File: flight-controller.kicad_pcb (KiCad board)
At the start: 4 copper layers, 36 x 36 mm, 61 parts, among them J1 USB_C_Receptacle_USB2.0, Q1 AO3400A, SW1 SW_Push, U1 AT32F435RGT7, U2 BMI270, U3 BMP280, U4 W25N01GVZEIG, U5 AT7456E, U6 TPS54302, U7 TPS54302, U8 TLV75733PDBV, U9 USBLC6-2P6

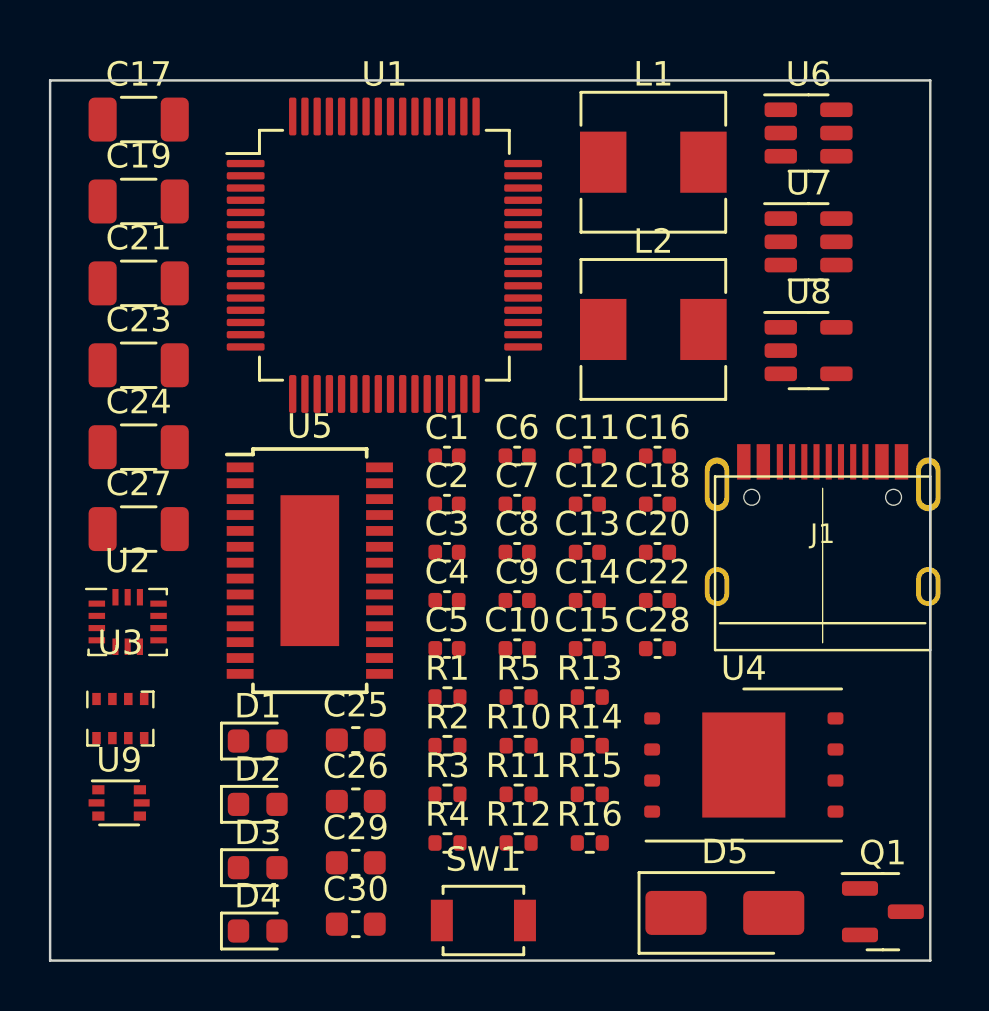
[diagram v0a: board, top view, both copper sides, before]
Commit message: Add 3D model for USB C, add speculative board and pad shapes
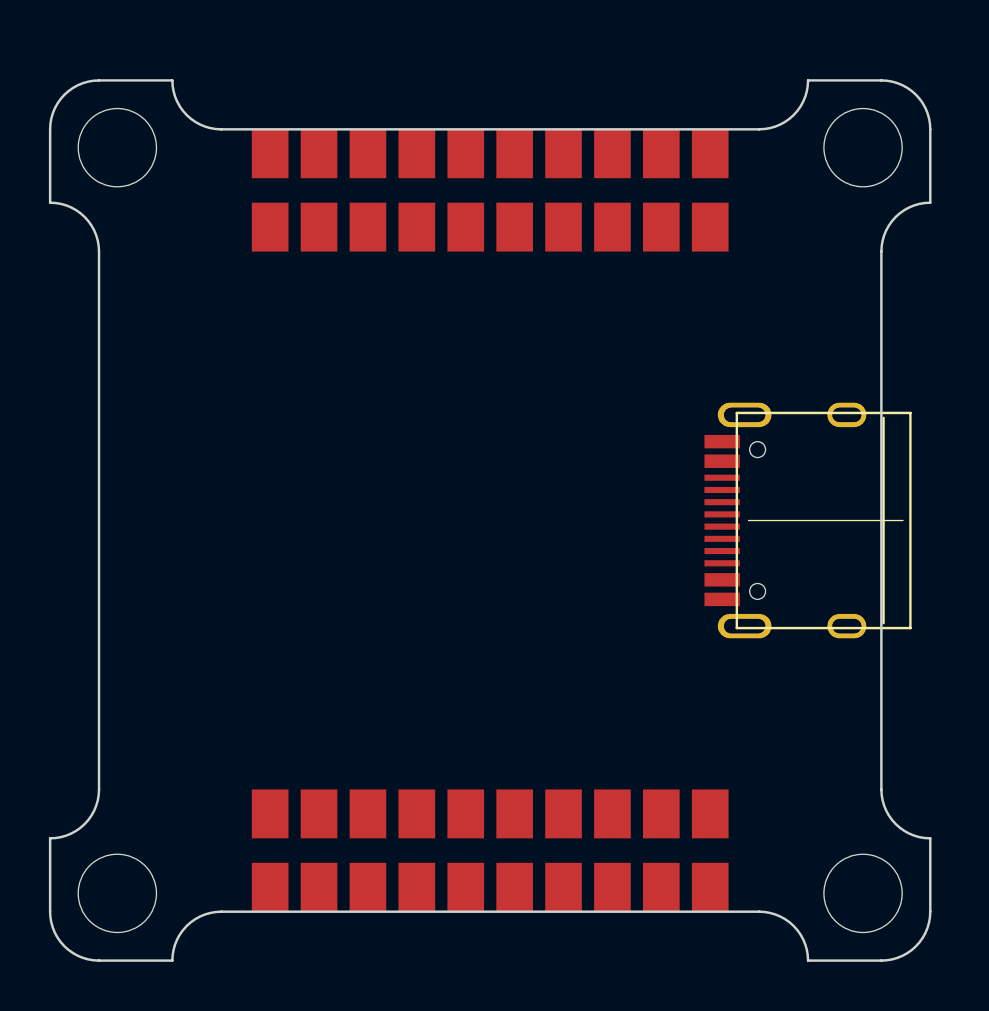
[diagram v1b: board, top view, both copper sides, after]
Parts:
- removed C1, C10, C11, C12, C13, C14, C15, C18, C2, C20, C28, C3, C4, C5, C6, C7, C8, C9: 100n, Capacitor_SMD:C_0402_1005Metric
- removed C16, C22: 68p, Capacitor_SMD:C_0402_1005Metric
- removed C17, C23, C24, C27: 22u, Capacitor_SMD:C_1206_3216Metric
- removed C19, C21: 10u 50V, Capacitor_SMD:C_1206_3216Metric
- removed C25, C26, C29, C30: 10u, Capacitor_SMD:C_0603_1608Metric
- removed D1: BLUE, LED_SMD:LED_0603_1608Metric
- removed D2: GREEN, LED_SMD:LED_0603_1608Metric
- removed D3: RED, LED_SMD:LED_0603_1608Metric
- removed D4: YELLOW, LED_SMD:LED_0603_1608Metric
- removed D5: SS34, Diode_SMD:D_SMA
- removed L1, L2: 10u, Inductor_SMD:L_Sunlord_MWSA0503S
- removed Q1: AO3400A, Package_TO_SOT_SMD:SOT-23
- removed R1, R14, R4, R5: 10k, Resistor_SMD:R_0402_1005Metric
- removed R10, R12: 100k, Resistor_SMD:R_0402_1005Metric
- removed R11: 6.34k, Resistor_SMD:R_0402_1005Metric
- removed R13: 13.3k, Resistor_SMD:R_0402_1005Metric
- removed R15, R16: 75, Resistor_SMD:R_0402_1005Metric
- removed R2, R3: 5.1k, Resistor_SMD:R_0402_1005Metric
- removed SW1: SW_Push, Button_Switch_SMD:SW_SPST_B3U-1000P
- removed U1: AT32F435RGT7, Package_QFP:LQFP-64_10x10mm_P0.5mm
- removed U2: BMI270, Package_LGA:Bosch_LGA-14_3x2.5mm_P0.5mm
- removed U3: BMP280, Package_LGA:Bosch_LGA-8_2x2.5mm_P0.65mm_ClockwisePinNumbering
- removed U4: W25N01GVZEIG, Package_SON:WSON-8-1EP_8x6mm_P1.27mm_EP3.4x4.3mm
- removed U5: AT7456E, Package_SO:TSSOP-28-1EP_4.4x9.7mm_P0.65mm
- removed U6, U7: TPS54302, Package_TO_SOT_SMD:SOT-23-6
- removed U8: TLV75733PDBV, Package_TO_SOT_SMD:SOT-23-5
- removed U9: USBLC6-2P6, Package_TO_SOT_SMD:SOT-666
- added H1: MountingHole, MountingHole:MountingHole_3.2mm_M3, F.Cu at (102.8, 87.8)
- added H2: MountingHole, MountingHole:MountingHole_3.2mm_M3, F.Cu at (133.2, 87.8)
- added H3: MountingHole, MountingHole:MountingHole_3.2mm_M3, F.Cu at (102.8, 118.2)
- added H4: MountingHole, MountingHole:MountingHole_3.2mm_M3, F.Cu at (133.2, 118.2)
- added REF**: TestPoint_Pad_1.5x1.5mm, TestPoint:TestPoint_Pad_1.5x1.5mm, F.Cu at (109.0, 118.0)
- added REF**: TestPoint_Pad_1.5x1.5mm, TestPoint:TestPoint_Pad_1.5x1.5mm, F.Cu at (109.0, 88.0)
- added REF**: TestPoint_Pad_1.5x1.5mm, TestPoint:TestPoint_Pad_1.5x1.5mm, F.Cu at (125.0, 91.0)
- added REF**: TestPoint_Pad_1.5x1.5mm, TestPoint:TestPoint_Pad_1.5x1.5mm, F.Cu at (117.0, 118.0)
- added REF**: TestPoint_Pad_1.5x1.5mm, TestPoint:TestPoint_Pad_1.5x1.5mm, F.Cu at (121.0, 118.0)
- added REF**: TestPoint_Pad_1.5x1.5mm, TestPoint:TestPoint_Pad_1.5x1.5mm, F.Cu at (111.0, 88.0)
- added REF**: TestPoint_Pad_1.5x1.5mm, TestPoint:TestPoint_Pad_1.5x1.5mm, F.Cu at (113.0, 88.0)
- added REF**: TestPoint_Pad_1.5x1.5mm, TestPoint:TestPoint_Pad_1.5x1.5mm, F.Cu at (113.0, 118.0)
- added REF**: TestPoint_Pad_1.5x1.5mm, TestPoint:TestPoint_Pad_1.5x1.5mm, F.Cu at (115.0, 118.0)
- added REF**: TestPoint_Pad_1.5x1.5mm, TestPoint:TestPoint_Pad_1.5x1.5mm, F.Cu at (121.0, 91.0)
- added REF**: TestPoint_Pad_1.5x1.5mm, TestPoint:TestPoint_Pad_1.5x1.5mm, F.Cu at (111.0, 115.0)
- added REF**: TestPoint_Pad_1.5x1.5mm, TestPoint:TestPoint_Pad_1.5x1.5mm, F.Cu at (113.0, 115.0)
- added REF**: TestPoint_Pad_1.5x1.5mm, TestPoint:TestPoint_Pad_1.5x1.5mm, F.Cu at (125.0, 88.0)
- added REF**: TestPoint_Pad_1.5x1.5mm, TestPoint:TestPoint_Pad_1.5x1.5mm, F.Cu at (119.0, 91.0)
- added REF**: TestPoint_Pad_1.5x1.5mm, TestPoint:TestPoint_Pad_1.5x1.5mm, F.Cu at (119.0, 88.0)
- added REF**: TestPoint_Pad_1.5x1.5mm, TestPoint:TestPoint_Pad_1.5x1.5mm, F.Cu at (125.0, 118.0)
- added REF**: TestPoint_Pad_1.5x1.5mm, TestPoint:TestPoint_Pad_1.5x1.5mm, F.Cu at (115.0, 88.0)
- added REF**: TestPoint_Pad_1.5x1.5mm, TestPoint:TestPoint_Pad_1.5x1.5mm, F.Cu at (127.0, 115.0)
- added REF**: TestPoint_Pad_1.5x1.5mm, TestPoint:TestPoint_Pad_1.5x1.5mm, F.Cu at (109.0, 91.0)
- added REF**: TestPoint_Pad_1.5x1.5mm, TestPoint:TestPoint_Pad_1.5x1.5mm, F.Cu at (123.0, 88.0)
- added REF**: TestPoint_Pad_1.5x1.5mm, TestPoint:TestPoint_Pad_1.5x1.5mm, F.Cu at (119.0, 118.0)
- added REF**: TestPoint_Pad_1.5x1.5mm, TestPoint:TestPoint_Pad_1.5x1.5mm, F.Cu at (111.0, 118.0)
- added REF**: TestPoint_Pad_1.5x1.5mm, TestPoint:TestPoint_Pad_1.5x1.5mm, F.Cu at (117.0, 88.0)
- added REF**: TestPoint_Pad_1.5x1.5mm, TestPoint:TestPoint_Pad_1.5x1.5mm, F.Cu at (127.0, 91.0)
- added REF**: TestPoint_Pad_1.5x1.5mm, TestPoint:TestPoint_Pad_1.5x1.5mm, F.Cu at (117.0, 91.0)
- added REF**: TestPoint_Pad_1.5x1.5mm, TestPoint:TestPoint_Pad_1.5x1.5mm, F.Cu at (125.0, 115.0)
- added REF**: TestPoint_Pad_1.5x1.5mm, TestPoint:TestPoint_Pad_1.5x1.5mm, F.Cu at (127.0, 118.0)
- added REF**: TestPoint_Pad_1.5x1.5mm, TestPoint:TestPoint_Pad_1.5x1.5mm, F.Cu at (111.0, 91.0)
- added REF**: TestPoint_Pad_1.5x1.5mm, TestPoint:TestPoint_Pad_1.5x1.5mm, F.Cu at (123.0, 91.0)
- added REF**: TestPoint_Pad_1.5x1.5mm, TestPoint:TestPoint_Pad_1.5x1.5mm, F.Cu at (117.0, 115.0)
- added REF**: TestPoint_Pad_1.5x1.5mm, TestPoint:TestPoint_Pad_1.5x1.5mm, F.Cu at (123.0, 115.0)
- added REF**: TestPoint_Pad_1.5x1.5mm, TestPoint:TestPoint_Pad_1.5x1.5mm, F.Cu at (121.0, 88.0)
- added REF**: TestPoint_Pad_1.5x1.5mm, TestPoint:TestPoint_Pad_1.5x1.5mm, F.Cu at (127.0, 88.0)
- added REF**: TestPoint_Pad_1.5x1.5mm, TestPoint:TestPoint_Pad_1.5x1.5mm, F.Cu at (113.0, 91.0)
- added REF**: TestPoint_Pad_1.5x1.5mm, TestPoint:TestPoint_Pad_1.5x1.5mm, F.Cu at (121.0, 115.0)
- added REF**: TestPoint_Pad_1.5x1.5mm, TestPoint:TestPoint_Pad_1.5x1.5mm, F.Cu at (123.0, 118.0)
- added REF**: TestPoint_Pad_1.5x1.5mm, TestPoint:TestPoint_Pad_1.5x1.5mm, F.Cu at (115.0, 115.0)
- added REF**: TestPoint_Pad_1.5x1.5mm, TestPoint:TestPoint_Pad_1.5x1.5mm, F.Cu at (109.0, 115.0)
- added REF**: TestPoint_Pad_1.5x1.5mm, TestPoint:TestPoint_Pad_1.5x1.5mm, F.Cu at (115.0, 91.0)
- added REF**: TestPoint_Pad_1.5x1.5mm, TestPoint:TestPoint_Pad_1.5x1.5mm, F.Cu at (119.0, 115.0)
- moved J1 2.88 mm to (132.6, 103.0), turned to 90 degrees
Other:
- outline, holes or cut-outs redrawn

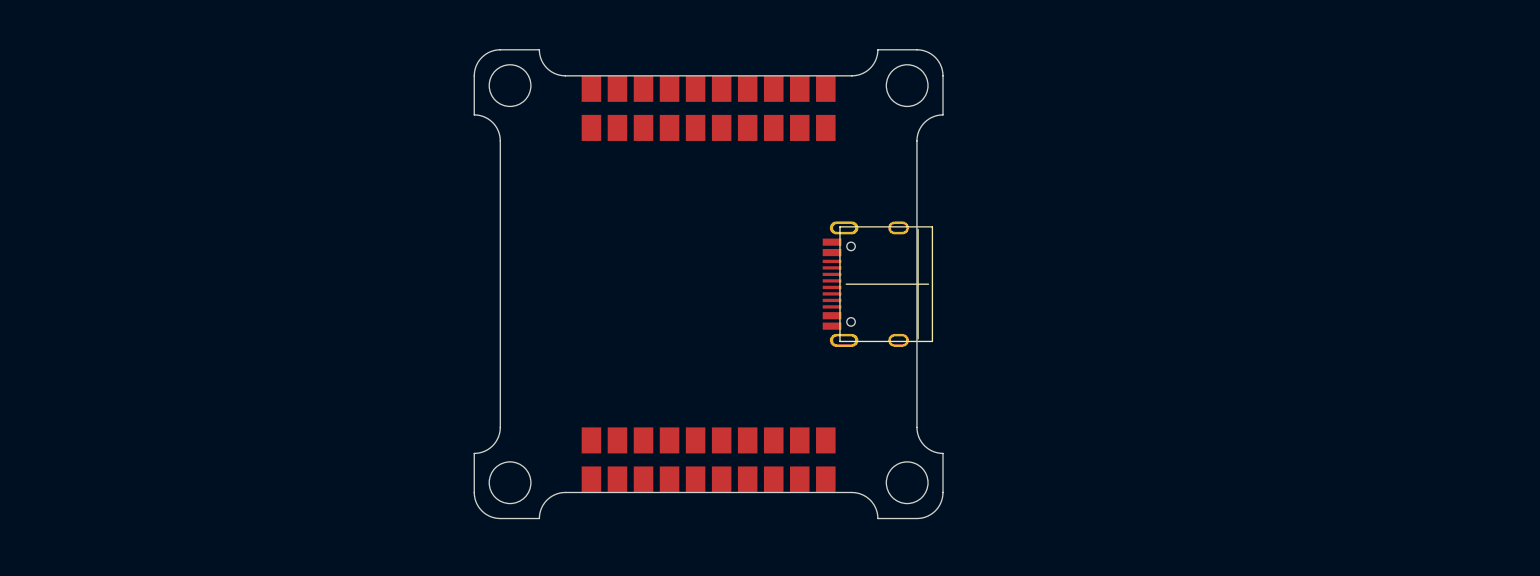
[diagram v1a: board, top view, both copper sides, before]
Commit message: Add voltage sense divider, rework board shape
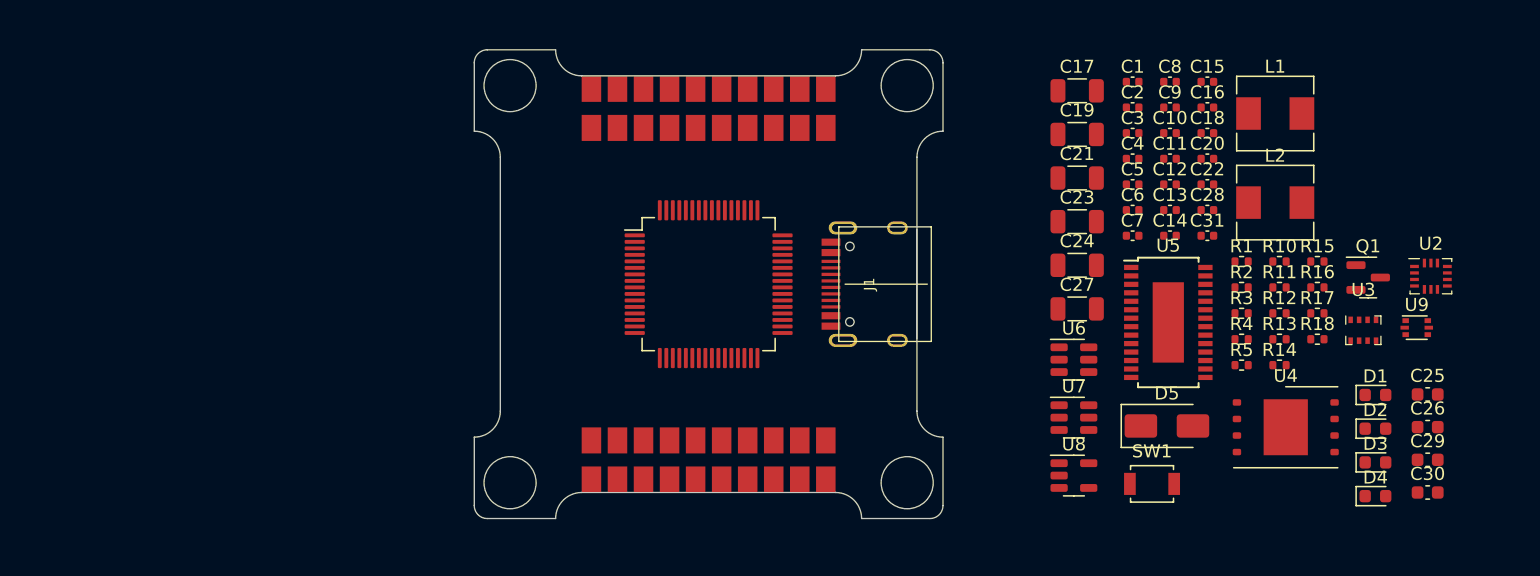
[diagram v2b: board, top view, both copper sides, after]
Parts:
- added C1: 100n, Capacitor_SMD:C_0402_1005Metric, F.Cu at (150.6, 87.5)
- added C10: 100n, Capacitor_SMD:C_0402_1005Metric, F.Cu at (153.4, 91.4)
- added C11: 100n, Capacitor_SMD:C_0402_1005Metric, F.Cu at (153.4, 93.4)
- added C12: 100n, Capacitor_SMD:C_0402_1005Metric, F.Cu at (153.4, 95.3)
- added C13: 100n, Capacitor_SMD:C_0402_1005Metric, F.Cu at (153.4, 97.3)
- added C14: 100n, Capacitor_SMD:C_0402_1005Metric, F.Cu at (153.4, 99.3)
- added C15: 100n, Capacitor_SMD:C_0402_1005Metric, F.Cu at (156.3, 87.5)
- added C16: 68p, Capacitor_SMD:C_0402_1005Metric, F.Cu at (156.3, 89.4)
- added C17: 22u, Capacitor_SMD:C_1206_3216Metric, F.Cu at (146.3, 88.2)
- added C18: 100n, Capacitor_SMD:C_0402_1005Metric, F.Cu at (156.3, 91.4)
- added C19: 10u 50V, Capacitor_SMD:C_1206_3216Metric, F.Cu at (146.3, 91.5)
- added C2: 100n, Capacitor_SMD:C_0402_1005Metric, F.Cu at (150.6, 89.4)
- added C20: 100n, Capacitor_SMD:C_0402_1005Metric, F.Cu at (156.3, 93.4)
- added C21: 10u 50V, Capacitor_SMD:C_1206_3216Metric, F.Cu at (146.3, 94.8)
- added C22: 68p, Capacitor_SMD:C_0402_1005Metric, F.Cu at (156.3, 95.3)
- added C23: 22u, Capacitor_SMD:C_1206_3216Metric, F.Cu at (146.3, 98.2)
- added C24: 22u, Capacitor_SMD:C_1206_3216Metric, F.Cu at (146.3, 101.5)
- added C25: 10u, Capacitor_SMD:C_0603_1608Metric, F.Cu at (173.2, 111.5)
- added C26: 10u, Capacitor_SMD:C_0603_1608Metric, F.Cu at (173.2, 114.0)
- added C27: 22u, Capacitor_SMD:C_1206_3216Metric, F.Cu at (146.3, 104.9)
- added C28: 100n, Capacitor_SMD:C_0402_1005Metric, F.Cu at (156.3, 97.3)
- added C29: 10u, Capacitor_SMD:C_0603_1608Metric, F.Cu at (173.2, 116.5)
- added C3: 100n, Capacitor_SMD:C_0402_1005Metric, F.Cu at (150.6, 91.4)
- added C30: 10u, Capacitor_SMD:C_0603_1608Metric, F.Cu at (173.2, 119.0)
- added C31: 100n, Capacitor_SMD:C_0402_1005Metric, F.Cu at (156.3, 99.3)
- added C4: 100n, Capacitor_SMD:C_0402_1005Metric, F.Cu at (150.6, 93.4)
- added C5: 100n, Capacitor_SMD:C_0402_1005Metric, F.Cu at (150.6, 95.3)
- added C6: 100n, Capacitor_SMD:C_0402_1005Metric, F.Cu at (150.6, 97.3)
- added C7: 100n, Capacitor_SMD:C_0402_1005Metric, F.Cu at (150.6, 99.3)
- added C8: 100n, Capacitor_SMD:C_0402_1005Metric, F.Cu at (153.4, 87.5)
- added C9: 100n, Capacitor_SMD:C_0402_1005Metric, F.Cu at (153.4, 89.4)
- added D1: BLUE, LED_SMD:LED_0603_1608Metric, F.Cu at (169.2, 111.5)
- added D2: GREEN, LED_SMD:LED_0603_1608Metric, F.Cu at (169.2, 114.1)
- added D3: RED, LED_SMD:LED_0603_1608Metric, F.Cu at (169.2, 116.7)
- added D4: YELLOW, LED_SMD:LED_0603_1608Metric, F.Cu at (169.2, 119.3)
- added D5: SS34, Diode_SMD:D_SMA, F.Cu at (153.2, 113.9)
- added L1: 10u, Inductor_SMD:L_Sunlord_MWSA0503S, F.Cu at (161.5, 89.9)
- added L2: 10u, Inductor_SMD:L_Sunlord_MWSA0503S, F.Cu at (161.5, 96.7)
- added Q1: AO3400A, Package_TO_SOT_SMD:SOT-23, F.Cu at (168.7, 102.5)
- added R1: 10k, Resistor_SMD:R_0402_1005Metric, F.Cu at (158.9, 101.3)
- added R10: 100k, Resistor_SMD:R_0402_1005Metric, F.Cu at (161.8, 101.3)
- added R11: 6.34k, Resistor_SMD:R_0402_1005Metric, F.Cu at (161.8, 103.2)
- added R12: 100k, Resistor_SMD:R_0402_1005Metric, F.Cu at (161.8, 105.2)
- added R13: 13.3k, Resistor_SMD:R_0402_1005Metric, F.Cu at (161.8, 107.2)
- added R14: 10k, Resistor_SMD:R_0402_1005Metric, F.Cu at (161.8, 109.2)
- added R15: 75, Resistor_SMD:R_0402_1005Metric, F.Cu at (164.8, 101.3)
- added R16: 75, Resistor_SMD:R_0402_1005Metric, F.Cu at (164.8, 103.2)
- added R17: 100k, Resistor_SMD:R_0402_1005Metric, F.Cu at (164.8, 105.2)
- added R18: 10k, Resistor_SMD:R_0402_1005Metric, F.Cu at (164.8, 107.2)
- added R2: 5.1k, Resistor_SMD:R_0402_1005Metric, F.Cu at (158.9, 103.2)
- added R3: 5.1k, Resistor_SMD:R_0402_1005Metric, F.Cu at (158.9, 105.2)
- added R4: 10k, Resistor_SMD:R_0402_1005Metric, F.Cu at (158.9, 107.2)
- added R5: 10k, Resistor_SMD:R_0402_1005Metric, F.Cu at (158.9, 109.2)
- added SW1: SW_Push, Button_Switch_SMD:SW_SPST_B3U-1000P, F.Cu at (152.1, 118.3)
- added U1: AT32F435RGT7, Package_QFP:LQFP-64_10x10mm_P0.5mm, F.Cu at (118.0, 103.0)
- added U2: BMI270, Package_LGA:Bosch_LGA-14_3x2.5mm_P0.5mm, F.Cu at (173.5, 102.4)
- added U3: BMP280, Package_LGA:Bosch_LGA-8_2x2.5mm_P0.65mm_ClockwisePinNumbering, F.Cu at (168.3, 106.5)
- added U4: W25N01GVZEIG, Package_SON:WSON-8-1EP_8x6mm_P1.27mm_EP3.4x4.3mm, F.Cu at (162.3, 114.0)
- added U5: AT7456E, Package_SO:TSSOP-28-1EP_4.4x9.7mm_P0.65mm, F.Cu at (153.3, 105.9)
- added U6: TPS54302, Package_TO_SOT_SMD:SOT-23-6, F.Cu at (146.1, 108.8)
- added U7: TPS54302, Package_TO_SOT_SMD:SOT-23-6, F.Cu at (146.1, 113.2)
- added U8: TLV75733PDBV, Package_TO_SOT_SMD:SOT-23-5, F.Cu at (146.1, 117.7)
- added U9: USBLC6-2P6, Package_TO_SOT_SMD:SOT-666, F.Cu at (172.4, 106.3)
- H1, H2, H3, H4: footprint MountingHole:MountingHole_3.2mm_M3 -> MountingHole:MountingHole_4mm
- moved J1 0.09 mm to (132.5, 103.0)
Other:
- outline, holes or cut-outs redrawn

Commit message: Add OSD crystal, minor changes to PCB
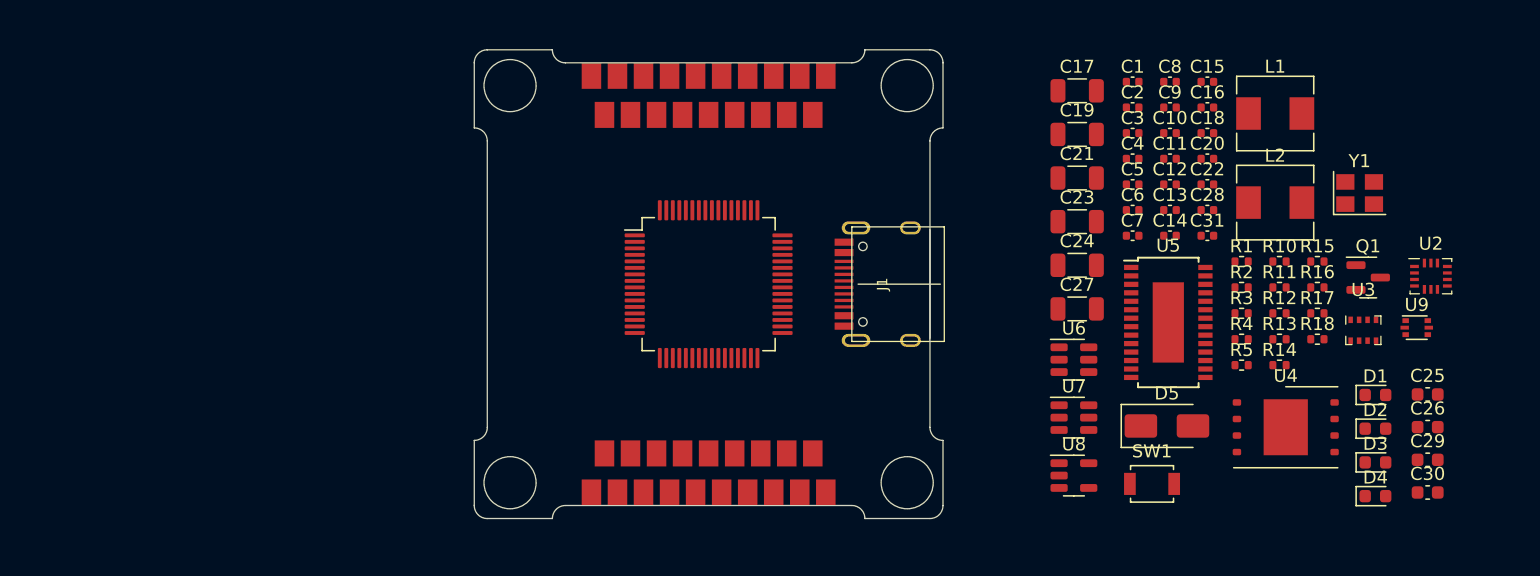
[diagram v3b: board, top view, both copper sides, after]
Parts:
- removed the REF** at (127.0, 115.0)
- removed the REF** at (127.0, 91.0)
- added Y1: 27MHz, Crystal:Crystal_SMD_3225-4Pin_3.2x2.5mm, F.Cu at (168.0, 96.0)
- moved REF** 1.41 mm to (126.0, 90.0)
- moved REF** 1.41 mm to (122.0, 90.0)
- moved REF** 1.41 mm to (112.0, 116.0)
- moved REF** 1.41 mm to (114.0, 116.0)
- moved REF** 1.41 mm to (120.0, 90.0)
- moved REF** 1.41 mm to (110.0, 90.0)
- moved REF** 1.41 mm to (118.0, 90.0)
- moved REF** 1.41 mm to (126.0, 116.0)
- moved REF** 1.41 mm to (112.0, 90.0)
- moved REF** 1.41 mm to (124.0, 90.0)
- moved REF** 1.41 mm to (118.0, 116.0)
- moved REF** 1.41 mm to (124.0, 116.0)
- moved REF** 1.41 mm to (122.0, 116.0)
- moved REF** 1.41 mm to (114.0, 90.0)
- moved REF** 1.41 mm to (116.0, 116.0)
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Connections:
- U4 pad 3: unconnected-(U4-IO2-Pad3) -> +3V3
- U4 pad 7: unconnected-(U4-IO3-Pad7) -> +3V3
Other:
- outline, holes or cut-outs redrawn
